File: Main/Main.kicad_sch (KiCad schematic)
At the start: 76 parts, among them J1 Conn_02x16_Odd_Even, J2 TYPE-C 6P, Q3 S9013 J3(RANGE:200-350), SW2 SS-12D11G3R, U1 BQ24074RGT, U2 DRV8833PW, U3 HUSB237-AA001-DN06R, U4 RT9742GGJ5, U5 RT9742GGJ5, U6 INA219AxDCN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

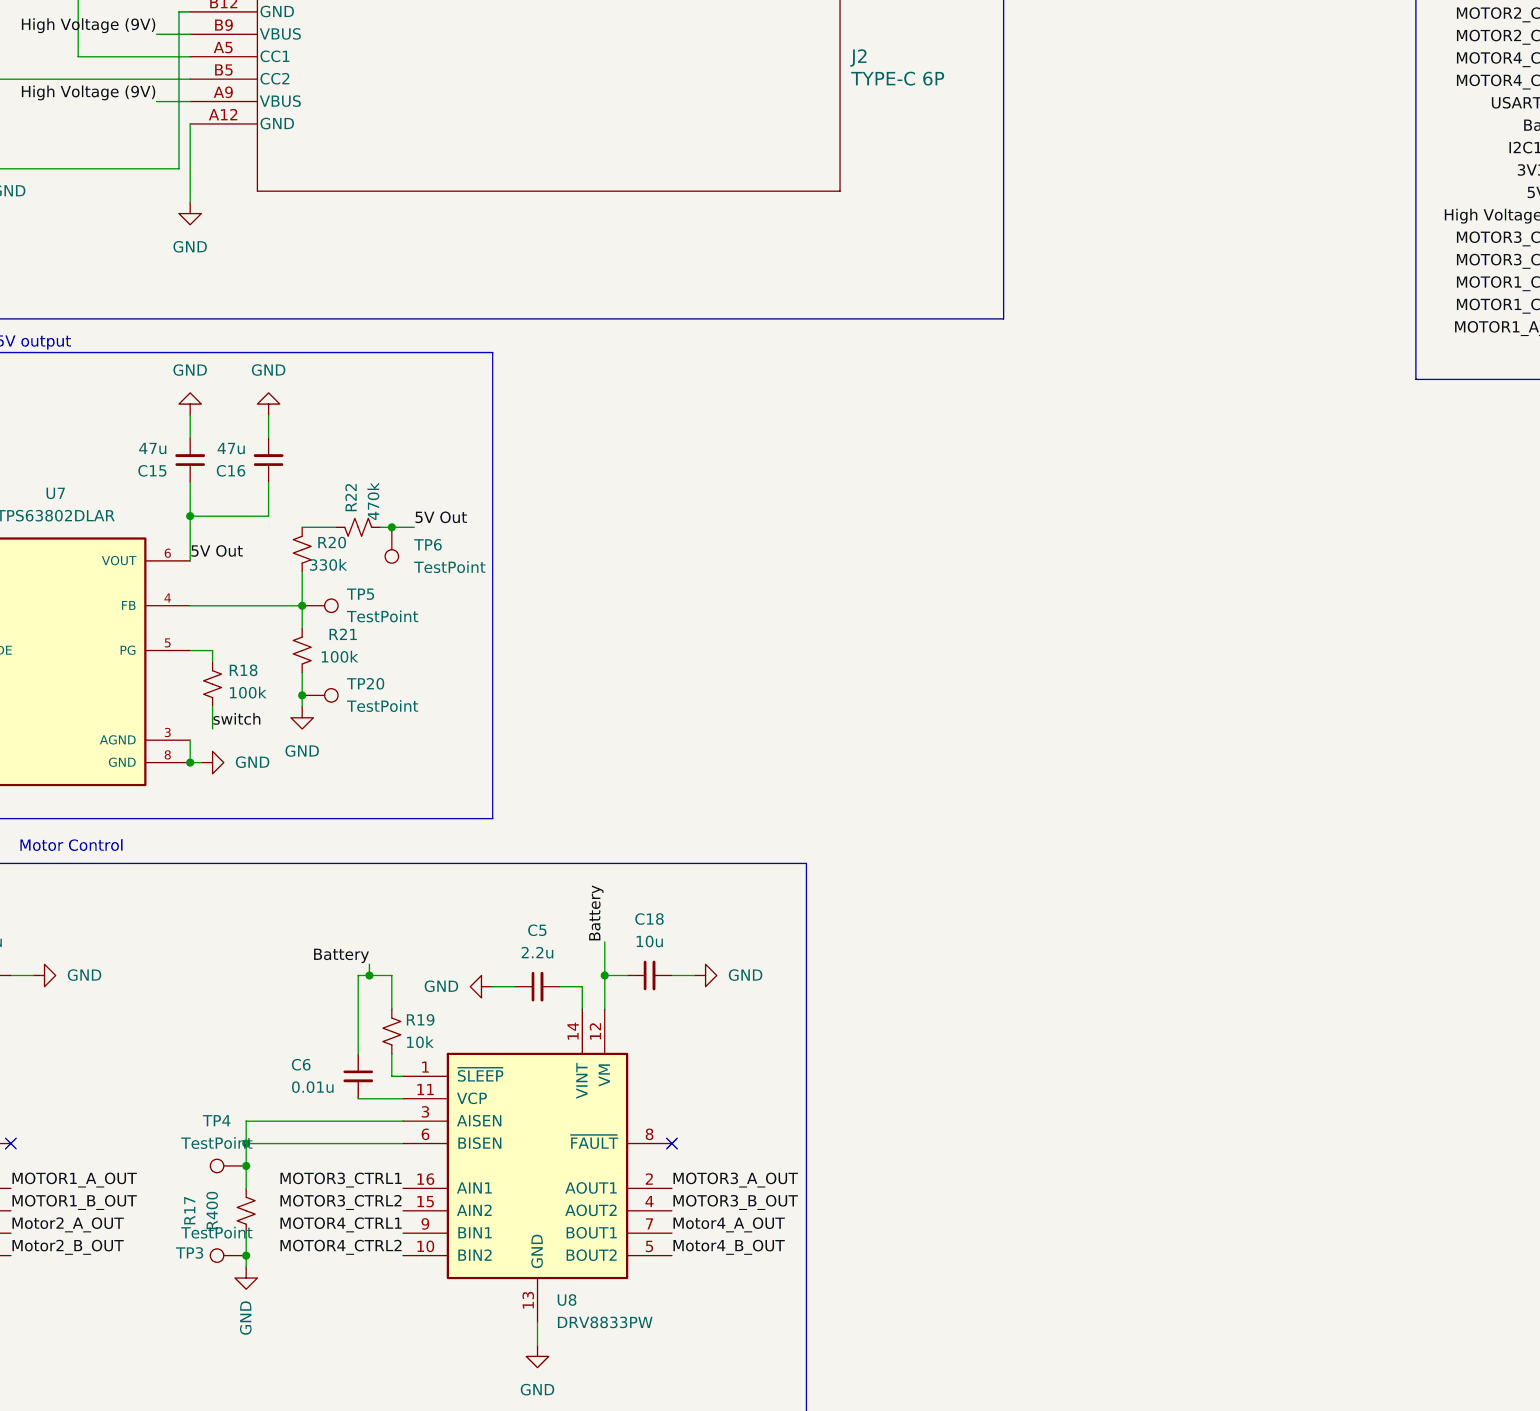
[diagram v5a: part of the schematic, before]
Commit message: connected other motor
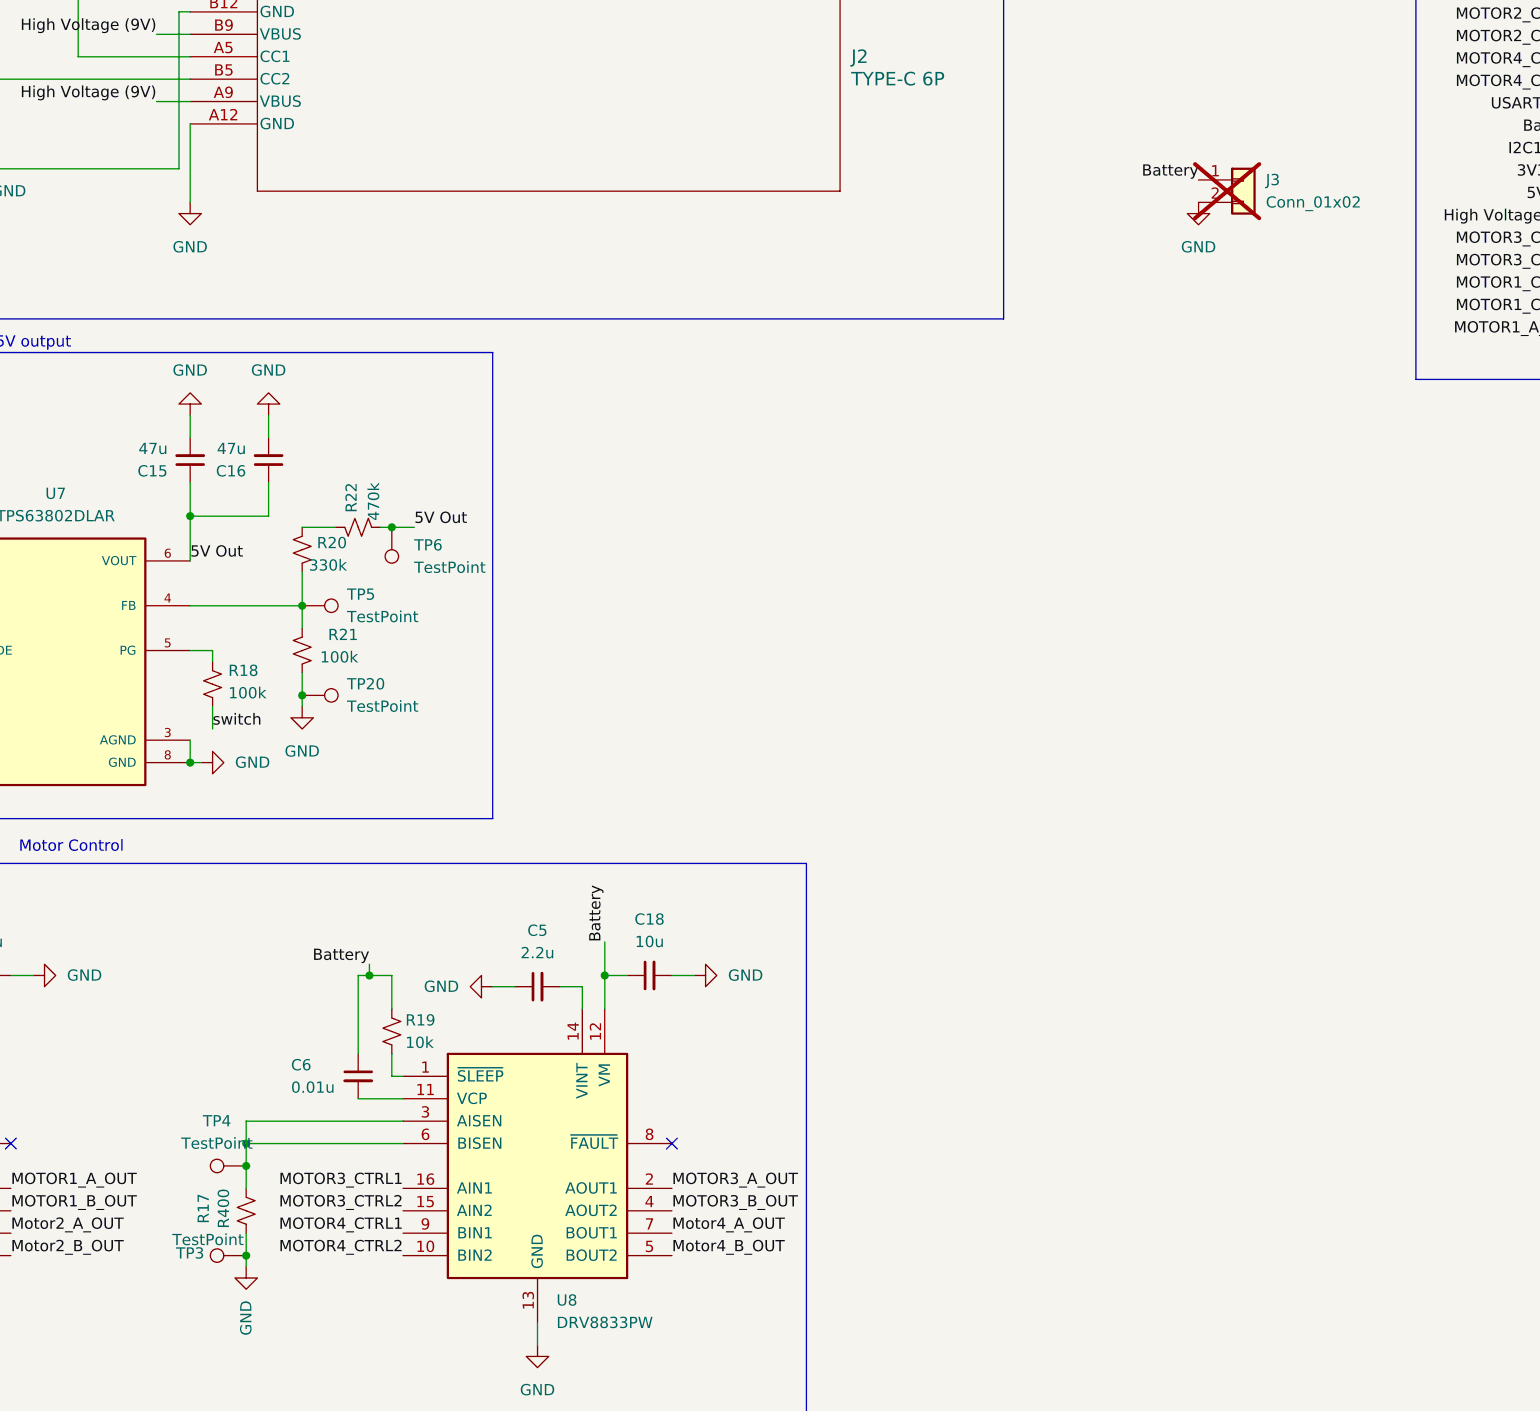
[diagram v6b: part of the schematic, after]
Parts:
- added J3: Conn_01x02, Connector_JST:JST_PH_S2B-PH-K_1x02_P2.00mm_Horizontal, symbol Connector_Generic:Conn_01x02
- TP1, TP10, TP11, TP12, TP13, TP14, TP15, TP16, TP17, TP18, TP19, TP2, TP20, TP3, TP4, TP5, TP6, TP7, TP8, TP9: footprint TestPoint:TestPoint_Pad_D3.0mm -> TestPoint:TestPoint_Pad_D1.0mm
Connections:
- net Battery: now also J3.1 (Pin_1)
- net GND: now also J3.2 (Pin_2)
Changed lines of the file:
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@@
 	)
 	(label "Battery"
+		(at 308.61 50.8 180)
+		(effects
+			(font
+				(size 1.27 1.27)
+			)
+			(justify right bottom)
+		)
+	)
+	(label "Battery"
 		(at 116.84 40.64 0)
 		(effects
@@
 			)
 		)
-		(property "Footprint" "TestPoint:TestPoint_Pad_D3.0mm"
+		(property "Footprint" "TestPoint:TestPoint_Pad_D1.0mm"
 			(at 76.2 83.82 0)
 			(effects
@@
 			)
 		)
-		(property "Footprint" "TestPoint:TestPoint_Pad_D3.0mm"
+		(property "Footprint" "TestPoint:TestPoint_Pad_D1.0mm"
 			(at 140.97 213.36 0)
 			(effects
@@
 	(symbol
 		(lib_id "power:GND")
+		(at 308.61 53.34 0)
+		(unit 1)
+		(exclude_from_sim no)
+		(in_bom yes)
+		(on_board yes)
+		(dnp no)
+		(fields_autoplaced yes)
+		(property "Reference" "#PWR013"
+			(at 308.61 59.69 0)
+			(effects
+				(font
+					(size 1.27 1.27)
+				)
+				(hide yes)
+			)
+		)
+		(property "Value" "GND"
+			(at 308.61 58.42 0)
+			(effects
+				(font
+					(size 1.27 1.27)
+				)
+			)
+		)
+		(property "Footprint" ""
+			(at 308.61 53.34 0)
+			(effects
+				(font
+					(size 1.27 1.27)
+				)
+				(hide yes)
+			)
+		)
+		(property "Datasheet" ""
+			(at 308.61 53.34 0)
+			(effects
+				(font
+					(size 1.27 1.27)
+				)
+				(hide yes)
+			)
+		)
+		(property "Description" "Power symbol creates a global label with name \"GND\" , ground"
+			(at 308.61 53.34 0)
+			(effects
+				(font
+					(size 1.27 1.27)
+				)
+				(hide yes)
+			)
+		)
+		(pin "1"
+		)
+		(instances
+			(project "Main"
+				(path "/0f55449c-8e79-4f10-a328-a1bcb934c334"
+					(reference "#PWR013")
+					(unit 1)
+				)
+			)
+		)
+	)
+	(symbol
+		(lib_id "power:GND")
 		(at 207.01 110.49 0)
 		(mirror y)
@@
 			)
 		)
-		(property "Footprint" "TestPoint:TestPoint_Pad_D3.0mm"
+		(property "Footprint" "TestPoint:TestPoint_Pad_D1.0mm"
 			(at 144.78 39.37 0)
 			(effects
@@
 			)
 		)
-		(property "Footprint" "TestPoint:TestPoint_Pad_D3.0mm"
+		(property "Footprint" "TestPoint:TestPoint_Pad_D1.0mm"
 			(at 144.78 50.8 0)
 			(effects
@@
 			)
 		)
-		(property "Footprint" "TestPoint:TestPoint_Pad_D3.0mm"
+		(property "Footprint" "TestPoint:TestPoint_Pad_D1.0mm"
 			(at 125.73 158.75 0)
 			(effects
@@
 			)
 		)
-		(property "Footprint" "TestPoint:TestPoint_Pad_D3.0mm"
+		(property "Footprint" "TestPoint:TestPoint_Pad_D1.0mm"
 			(at 200.66 157.48 0)
 			(effects
@@
 	)
 	(symbol
+		(lib_id "Connector_Generic:Conn_01x02")
+		(at 313.69 50.8 0)
+		(unit 1)
+		(exclude_from_sim no)
+		(in_bom no)
+		(on_board yes)
+		(dnp yes)
+		(fields_autoplaced yes)
+		(property "Reference" "J3"
+			(at 316.23 50.7999 0)
+			(effects
+				(font
+					(size 1.27 1.27)
+				)
+				(justify left)
+			)
+		)
+		(property "Value" "Conn_01x02"
+			(at 316.23 53.3399 0)
+			(effects
+				(font
+					(size 1.27 1.27)
+				)
+				(justify left)
+			)
+		)
+		(property "Footprint" "Connector_JST:JST_PH_S2B-PH-K_1x02_P2.00mm_Horizontal"
+			(at 313.69 50.8 0)
+			(effects
+				(font
+					(size 1.27 1.27)
+				)
+				(hide yes)
+			)
+		)
+		(property "Datasheet" "~"
+			(at 313.69 50.8 0)
+			(effects
+				(font
+					(size 1.27 1.27)
+				)
+				(hide yes)
+			)
+		)
+		(property "Description" "Generic connector, single row, 01x02, script generated (kicad-library-utils/schlib/autogen/connector/)"
+			(at 313.69 50.8 0)
+			(effects
+				(font
+					(size 1.27 1.27)
+				)
+				(hide yes)
+			)
+		)
+		(pin "2"
+		)
+		(pin "1"
+		)
+		(instances
+			(project "Main"
+				(path "/0f55449c-8e79-4f10-a328-a1bcb934c334"
+					(reference "J3")
+					(unit 1)
+				)
+			)
+		)
+	)
+	(symbol
 		(lib_id "Device:R_US")
 		(at 105.41 71.12 0)
@@
 			)
 		)
-		(property "Footprint" "TestPoint:TestPoint_Pad_D3.0mm"
+		(property "Footprint" "TestPoint:TestPoint_Pad_D1.0mm"
 			(at 212.09 90.17 0)
 			(effects
@@
 			)
 		)
-		(property "Footprint" "TestPoint:TestPoint_Pad_D3.0mm"
+		(property "Footprint" "TestPoint:TestPoint_Pad_D1.0mm"
 			(at 60.96 58.42 0)
 			(effects
@@
 			)
 		)
-		(property "Footprint" "TestPoint:TestPoint_Pad_D3.0mm"
+		(property "Footprint" "TestPoint:TestPoint_Pad_D1.0mm"
 			(at 242.57 205.74 0)
 			(effects
@@
 		)
 		(property "Value" "TestPoint"
-			(at 197.358 170.18 90)
+			(at 196.342 170.942 90)
 			(effects
 				(font
@@
 			)
 		)
-		(property "Footprint" "TestPoint:TestPoint_Pad_D3.0mm"
+		(property "Footprint" "TestPoint:TestPoint_Pad_D1.0mm"
 			(at 200.66 167.64 0)
 			(effects
@@
 			)
 		)
-		(property "Footprint" "TestPoint:TestPoint_Pad_D3.0mm"
+		(property "Footprint" "TestPoint:TestPoint_Pad_D1.0mm"
 			(at 67.31 67.31 0)
 			(effects
@@
 			)
 		)
-		(property "Footprint" "TestPoint:TestPoint_Pad_D3.0mm"
+		(property "Footprint" "TestPoint:TestPoint_Pad_D1.0mm"
 			(at 67.31 52.07 0)
 			(effects
@@
 			)
 		)
-		(property "Footprint" "TestPoint:TestPoint_Pad_D3.0mm"
+		(property "Footprint" "TestPoint:TestPoint_Pad_D1.0mm"
 			(at 76.2 95.25 0)
 			(effects
@@
 			)
 		)
-		(property "Footprint" "TestPoint:TestPoint_Pad_D3.0mm"
+		(property "Footprint" "TestPoint:TestPoint_Pad_D1.0mm"
 			(at 243.84 232.41 0)
 			(effects
@@
 			)
 		)
-		(property "Footprint" "TestPoint:TestPoint_Pad_D3.0mm"
+		(property "Footprint" "TestPoint:TestPoint_Pad_D1.0mm"
 			(at 125.73 166.37 0)
 			(effects
@@
 			)
 		)
-		(property "Footprint" "TestPoint:TestPoint_Pad_D3.0mm"
+		(property "Footprint" "TestPoint:TestPoint_Pad_D1.0mm"
 			(at 233.68 205.74 0)
 			(effects
@@
 			)
 		)
-		(property "Footprint" "TestPoint:TestPoint_Pad_D3.0mm"
+		(property "Footprint" "TestPoint:TestPoint_Pad_D1.0mm"
 			(at 207.01 104.14 0)
 			(effects
@@
 			)
 		)
-		(property "Footprint" "TestPoint:TestPoint_Pad_D3.0mm"
+		(property "Footprint" "TestPoint:TestPoint_Pad_D1.0mm"
 			(at 207.01 114.3 0)
 			(effects
@@
 			)
 		)
-		(property "Footprint" "TestPoint:TestPoint_Pad_D3.0mm"
+		(property "Footprint" "TestPoint:TestPoint_Pad_D1.0mm"
 			(at 140.97 228.6 0)
 			(effects
@@
 		(on_board yes)
 		(dnp no)
-		(fields_autoplaced yes)
 		(property "Reference" "R17"
-			(at 194.31 167.64 90)
+			(at 195.834 167.386 90)
 			(effects
 				(font
@@
 		)
 		(property "Value" "R400"
-			(at 196.85 167.64 90)
+			(at 198.12 167.386 90)
 			(effects
 				(font
@@
 			)
 		)
-		(property "Footprint" "TestPoint:TestPoint_Pad_D3.0mm"
+		(property "Footprint" "TestPoint:TestPoint_Pad_D1.0mm"
 			(at 60.96 48.26 0)
 			(effects
